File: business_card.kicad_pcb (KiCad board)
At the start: 4 copper layers, 85.6 x 54 mm, 68 parts, among them J1 USB_C_Receptacle_USB2.0_14P, J10 CAP_TOUCH_RECT, J11 CAP_TOUCH_RECT, J12 CAP_TOUCH_RECT, J13 CAP_TOUCH_CIRC, J2 CAP_TOUCH_CIRC, J3 CAP_TOUCH_RECT, J4 CAP_TOUCH_RECT, J5 CAP_TOUCH_RECT, J6 CAP_TOUCH_RECT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

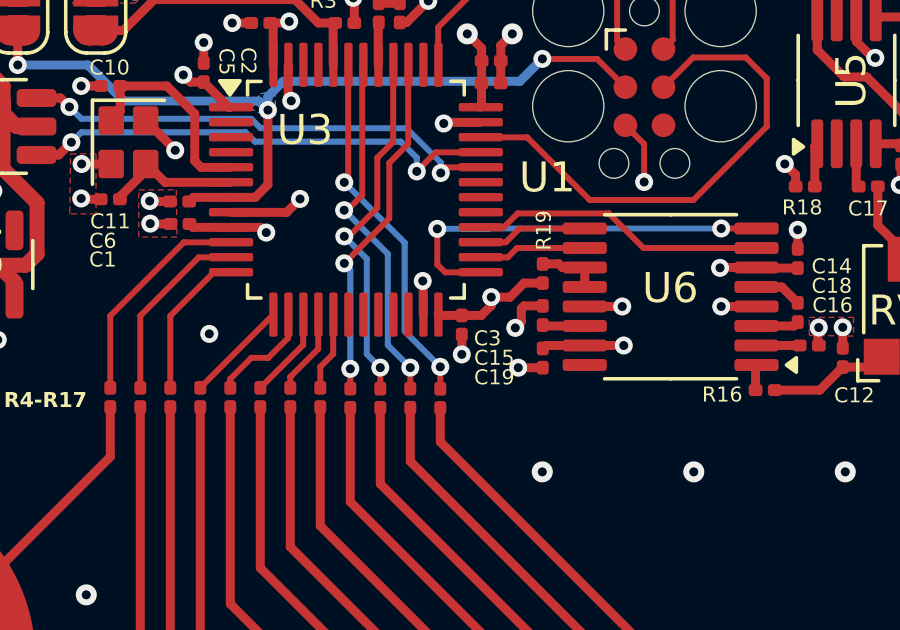
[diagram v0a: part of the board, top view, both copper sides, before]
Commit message: increase ic distance to .22mm
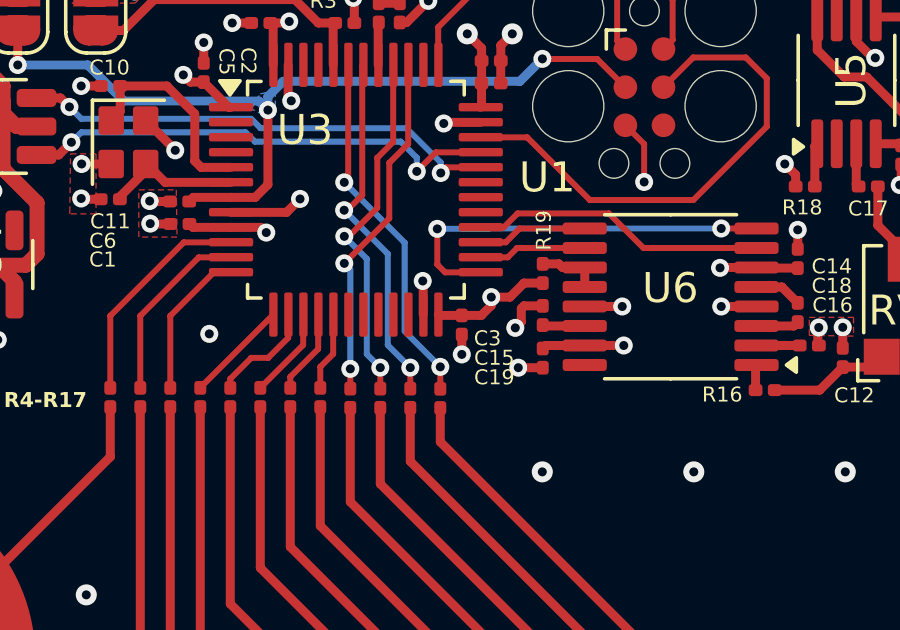
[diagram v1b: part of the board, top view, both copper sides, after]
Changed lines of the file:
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@@
 	)
 	(segment
-		(start 201.7025 80.11)
-		(end 201.68 80.0875)
-		(width 0.3)
-		(layer "F.Cu")
-		(net 2)
-	)
-	(segment
 		(start 203.45 79.5)
 		(end 204.075 79.5)
@@
 	)
 	(segment
+		(start 201.715 80.11)
+		(end 201.6875 80.0825)
+		(width 0.3)
+		(layer "F.Cu")
+		(net 2)
+	)
+	(segment
 		(start 212.29 78.5125)
 		(end 211.0875 78.5125)
@@
 	)
 	(segment
-		(start 202.4675 80.11)
-		(end 201.7025 80.11)
-		(width 0.3)
-		(layer "F.Cu")
-		(net 2)
-	)
-	(segment
 		(start 211.0875 78.5125)
 		(end 211.075 78.525)
@@
 	)
 	(segment
+		(start 202.4675 80.11)
+		(end 201.715 80.11)
+		(width 0.3)
+		(layer "F.Cu")
+		(net 2)
+	)
+	(segment
 		(start 196.665 70.3625)
 		(end 196.715 70.3125)
@@
 		(name "$teardrop_padvia$")
 		(hatch none 0.1)
-		(priority 30147)
-		(attr
-			(teardrop
-				(type padvia)
-			)
-		)
-		(connect_pads yes
-			(clearance 0)
-		)
-		(min_thickness 0.0254)
-		(filled_areas_thickness no)
-		(fill yes
-			(thermal_gap 0.5)
-			(thermal_bridge_width 0.5)
-			(island_removal_mode 1)
-			(island_area_min 10)
-		)
-		(polygon
-			(pts
-				(xy 202.0675 79.96) (xy 202.0675 80.26) (xy 202.296314 80.31) (xy 202.4685 80.11) (xy 202.296314 79.91)
-			)
-		)
-	)
-	(zone
-		(net 2)
-		(net_name "+3.3V")
-		(layer "F.Cu")
-		(name "$teardrop_padvia$")
-		(hatch none 0.1)
 		(priority 30032)
 		(attr
@@
 	)
 	(zone
+		(net 2)
+		(net_name "+3.3V")
+		(layer "F.Cu")
+		(name "$teardrop_padvia$")
+		(hatch none 0.1)
+		(priority 30000)
+		(attr
+			(teardrop
+				(type padvia)
+			)
+		)
+		(connect_pads yes
+			(clearance 0)
+		)
+		(min_thickness 0.0254)
+		(filled_areas_thickness no)
+		(fill yes
+			(thermal_gap 0.5)
+			(thermal_bridge_width 0.5)
+			(island_removal_mode 1)
+			(island_area_min 10)
+		)
+		(polygon
+			(pts
+				(xy 202.0675 79.96) (xy 202.0675 80.26) (xy 202.296314 80.31) (xy 202.4685 80.11) (xy 202.296314 79.91)
+			)
+		)
+	)
+	(zone
 		(net 3)
 		(net_name "+5V")
@@
 	)
 	(zone
-		(net 2)
-		(net_name "+3.3V")
-		(layer "F.Cu")
-		(name "$teardrop_padvia$")
-		(hatch none 0.1)
-		(priority 30150)
-		(attr
-			(teardrop
-				(type padvia)
-			)
-		)
-		(connect_pads yes
-			(clearance 0)
-		)
-		(min_thickness 0.0254)
-		(filled_areas_thickness no)
-		(fill yes
-			(thermal_gap 0.5)
-			(thermal_bridge_width 0.5)
-			(island_removal_mode 1)
-			(island_area_min 10)
-		)
-		(polygon
-			(pts
-				(xy 202.8675 80.26) (xy 202.8675 79.96) (xy 202.638686 79.91) (xy 202.4665 80.11) (xy 202.638686 80.31)
-			)
-		)
-	)
-	(zone
 		(net 3)
 		(net_name "+5V")
@@
 			)
 		)
+	)
+	(zone
+		(net 2)
+		(net_name "+3.3V")
+		(layer "F.Cu")
+		(name "$teardrop_padvia$")
+		(hatch none 0.1)
+		(priority 30000)
+		(attr
+			(teardrop
+				(type padvia)
+			)
+		)
+		(connect_pads yes
+			(clearance 0)
+		)
+		(min_thickness 0.0254)
+		(filled_areas_thickness no)
+		(fill yes
+			(thermal_gap 0.5)
+			(thermal_bridge_width 0.5)
+			(island_removal_mode 1)
+			(island_area_min 10)
+		)
+		(polygon
+			(pts
+				(xy 202.8675 80.26) (xy 202.8675 79.96) (xy 202.638686 79.91) (xy 202.4665 80.11) (xy 202.638686 80.31)
+			)
+		)

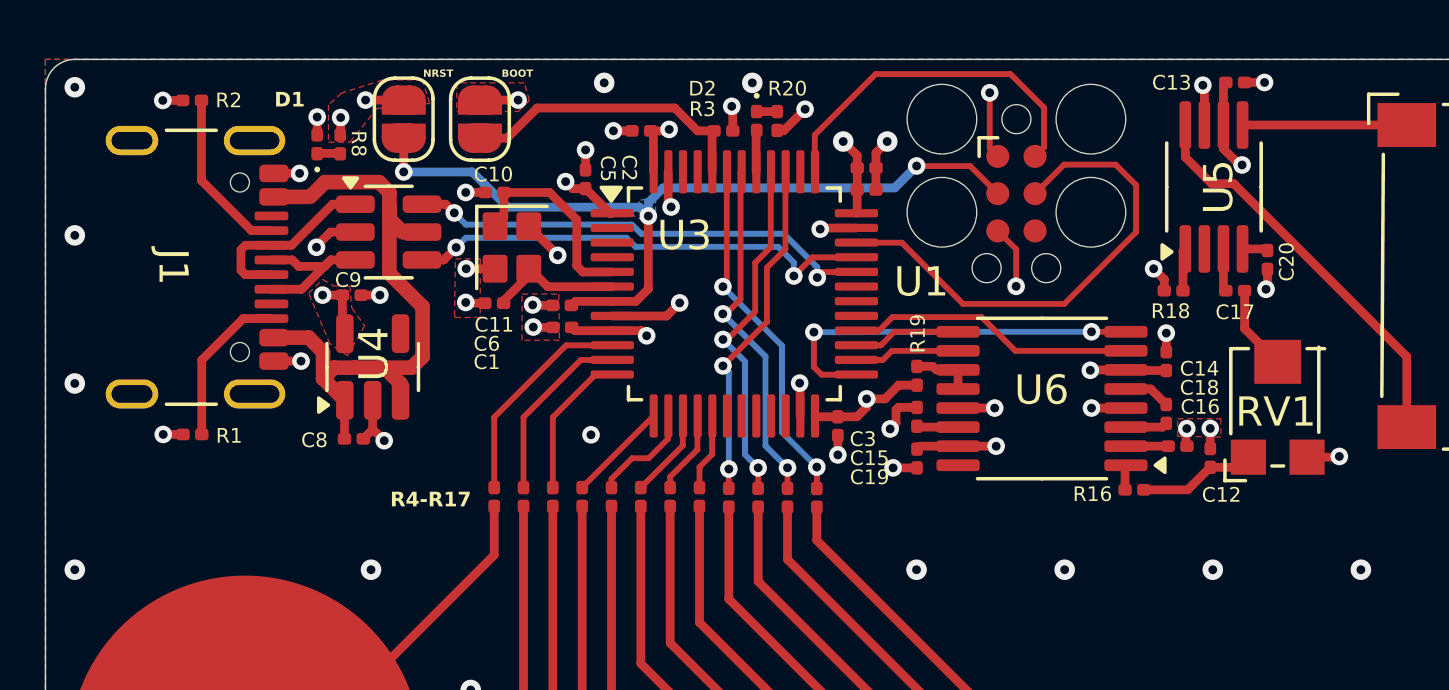
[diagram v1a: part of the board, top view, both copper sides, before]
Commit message: change IC distnace to .22mm
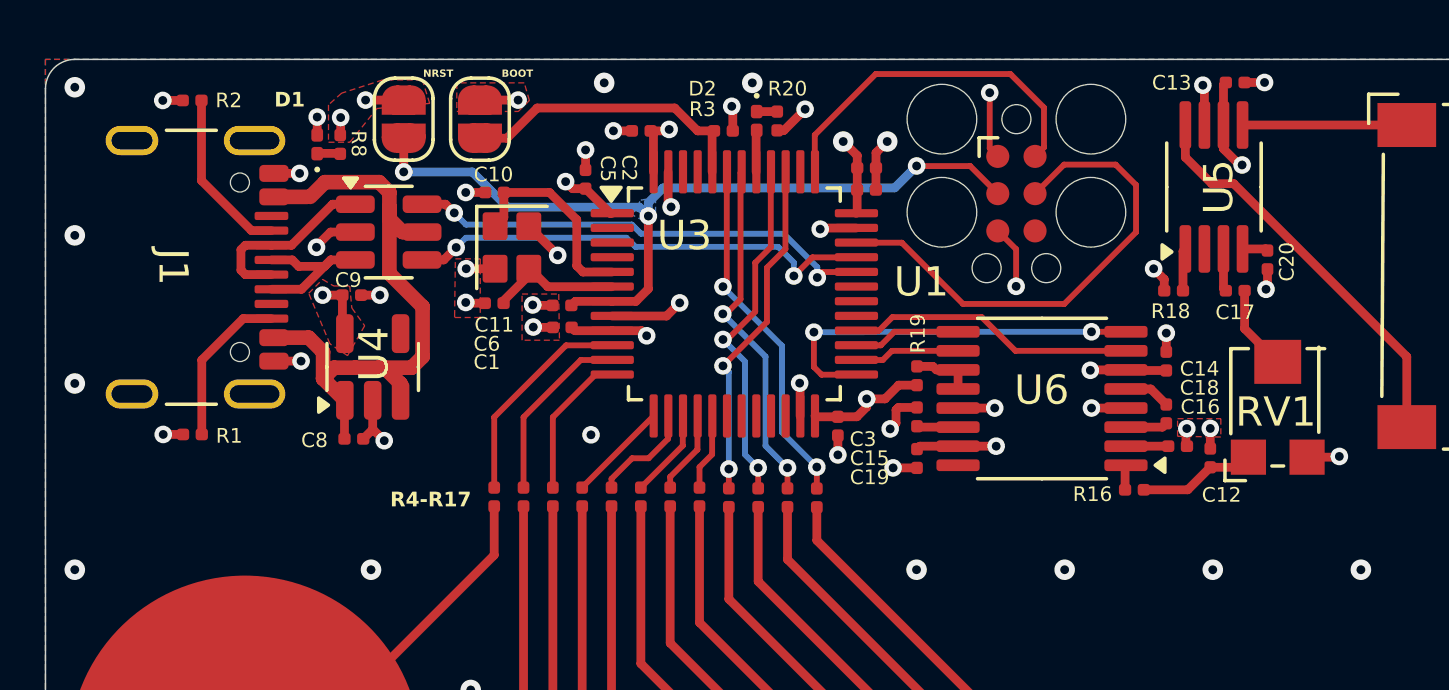
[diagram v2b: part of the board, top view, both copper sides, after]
